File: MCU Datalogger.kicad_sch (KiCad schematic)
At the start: 25 parts, among them U1 24LC1025, U2 24LC1025, U3 DS1337S_, U4 ATMEGA328P-AU, Y1 32.768 KHZ, Y2 16 MHz

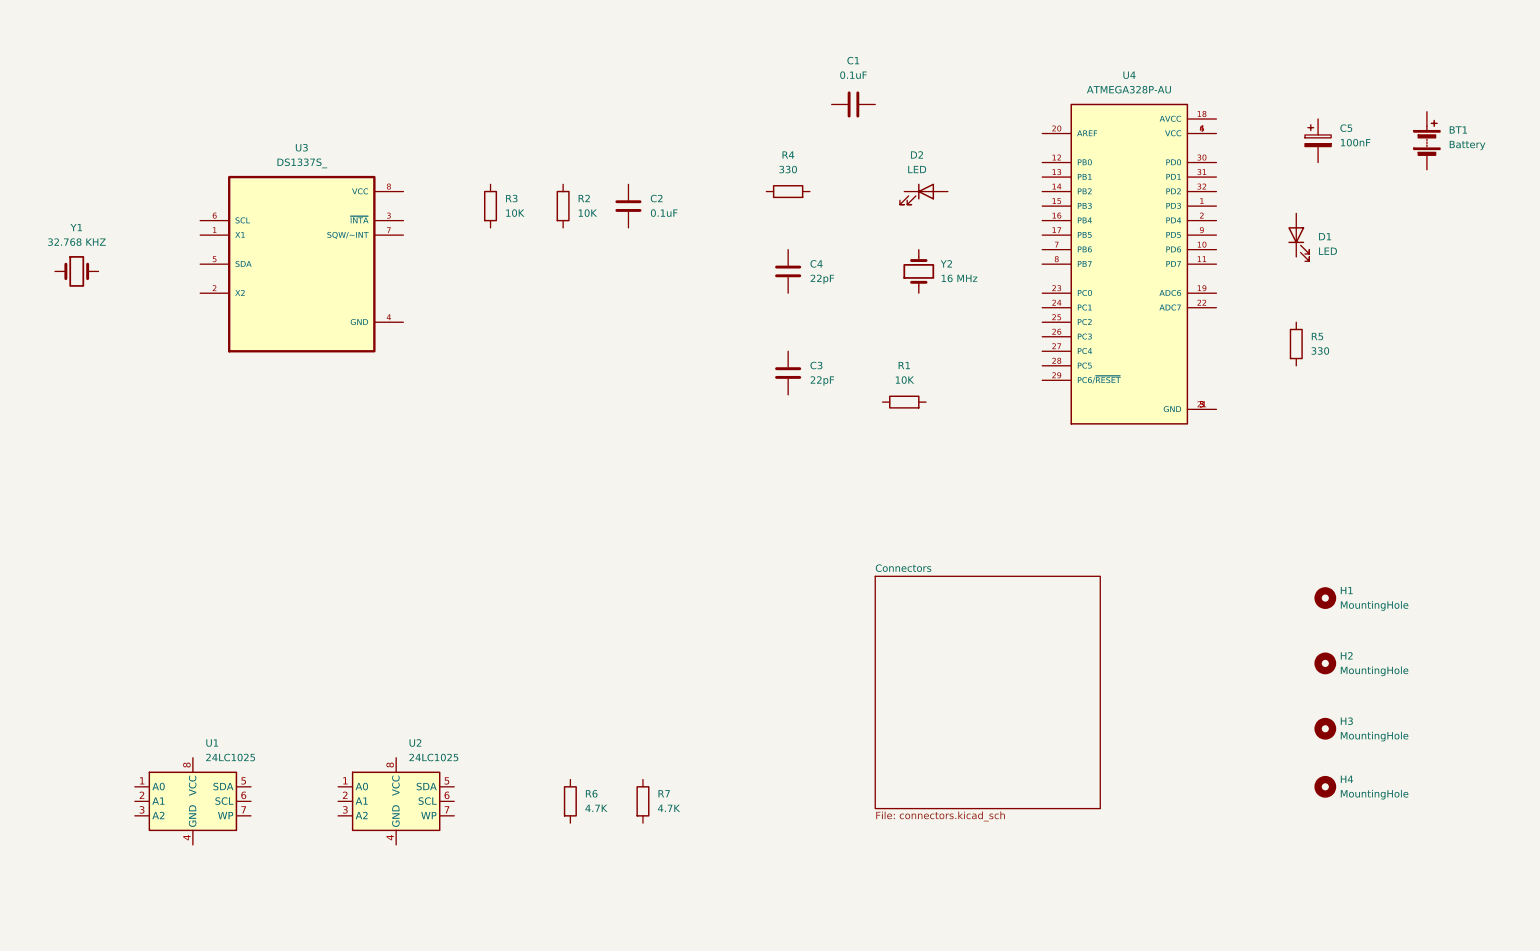
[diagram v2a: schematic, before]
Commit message: Completed wiring of main sheet.
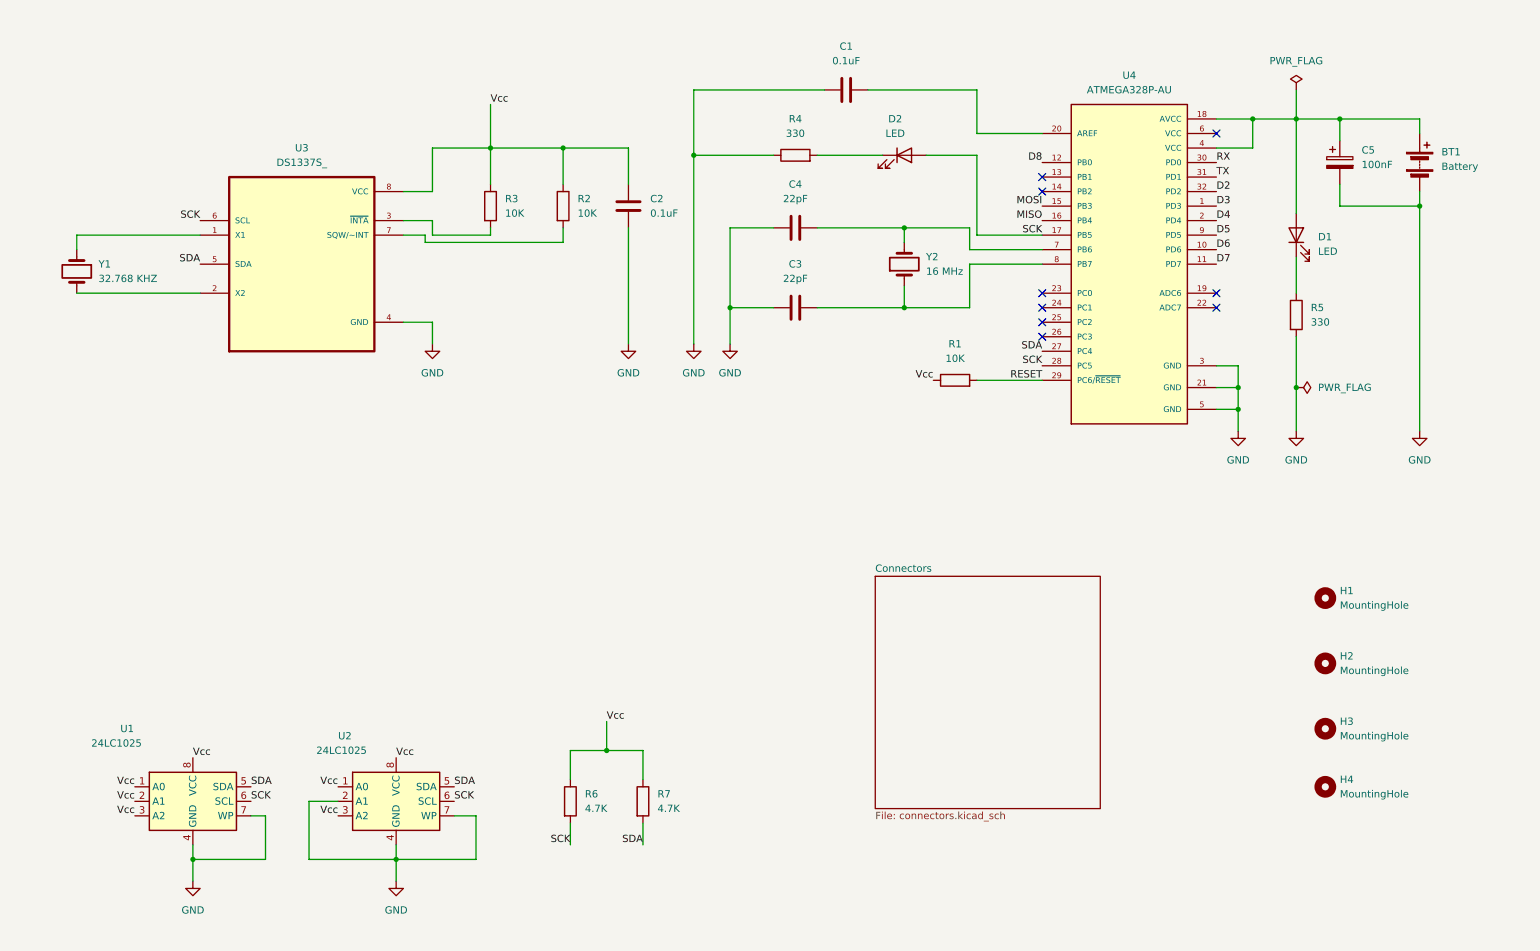
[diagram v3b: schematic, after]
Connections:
- net at R5.1: now also D1.1 (K)
- net GND: now reaches R5.2
- net GND: now also BT1.2 (-), C1.1, C2.2, C3.1, C4.1, C5.2, R4.1, U1.4 (GND), U1.7 (WP), U2.2 (A1), U2.4 (GND), U2.7 (WP), U3.4 (GND), U4.21 (GND), U4.3 (GND), U4.5 (GND)
- net Vcc: now reaches U2.1 (A0)
- net Vcc: now also C2.1, R1.1, R2.1, R3.1, R6.1, R7.1, U1.1 (A0), U1.2 (A1), U1.3 (A2), U1.8 (VCC), U2.3 (A2), U2.8 (VCC), U3.8 (VCC)
- net SDA: now reaches U2.5 (SDA)
- net SDA: now also R7.2, U1.5 (SDA), U3.5 (SDA), U4.27 (PC4)
- net SCK: now reaches U2.6 (SCL)
- net SCK: now also D2.2 (A), R6.2, U1.6 (SCL), U3.6 (SCL), U4.17 (PB5), U4.28 (PC5)
- net at R2.2: now also U3.7 (SQW/~INT)
- net at Y1.1: now also U3.1 (X1)
- net at Y1.2: now also U3.2 (X2)
- net at BT1.1 (+): now also C5.1, D1.2 (A), U4.18 (AVCC), U4.4 (VCC)
- net RESET: now reaches R1.2
- net RESET: now also U4.29 (PC6/~{RESET})
- net at D2.1 (K): now also R4.2
- net at C1.2: now also U4.20 (AREF)
- net at R3.2: now also U3.3 (~{INTA})
- net D3: now reaches U4.1 (PD3)
- net D6: now reaches U4.10 (PD6)
- net D7: now reaches U4.11 (PD7)
- net D8: now reaches U4.12 (PB0)
- net MOSI: now reaches U4.15 (PB3)
- net MISO: now reaches U4.16 (PB4)
- net D4: now reaches U4.2 (PD4)
- net RX: now reaches U4.30 (PD0)
- net TX: now reaches U4.31 (PD1)
- net D2: now reaches U4.32 (PD2)
- net at U4.6 (VCC): no longer U4.4 (VCC)
- net at U4.7 (PB6): now also C4.2, Y2.2
- net at U4.8 (PB7): now also C3.2, Y2.1
- net D5: now reaches U4.9 (PD5)
- no-connect marks 0 -> 9
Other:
- moved on the sheet: BT1, C1, C3, C4, C5, D2, R1, R4, R5, Y1, Y2

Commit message: Completed wiring in second sheet.
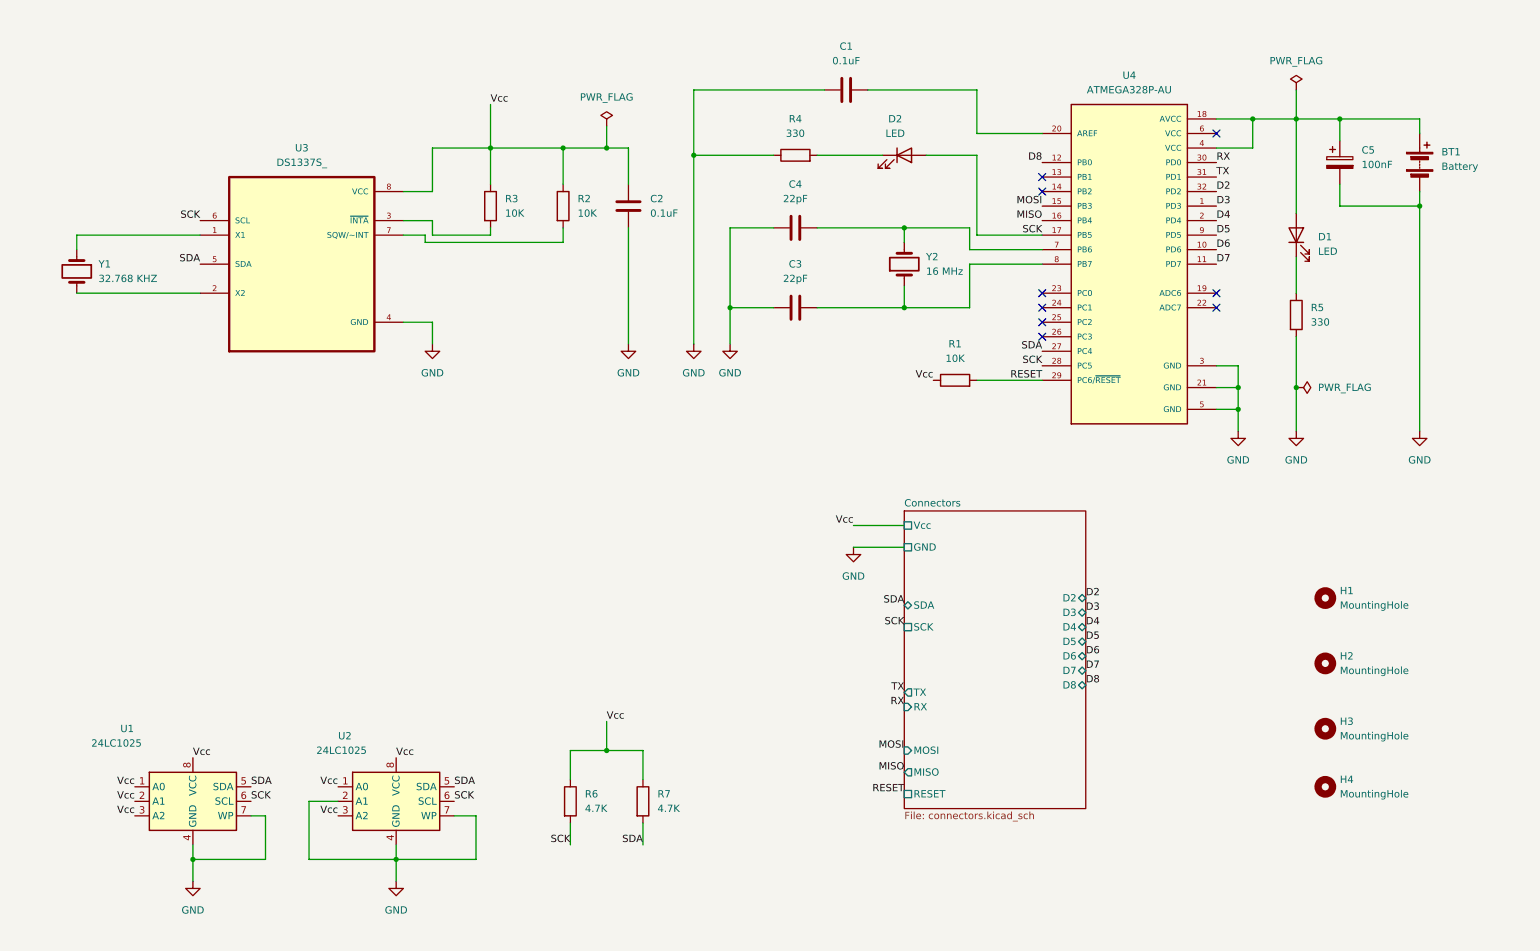
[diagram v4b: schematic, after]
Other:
- sheet Connectors ports: added D2, D3, D4, D5, D6, D7, D8, GND, MISO, MOSI, RESET, RX, SCK, SDA, TX, Vcc; removed none
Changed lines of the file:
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@@
   (junction (at 231.14 80.01) (diameter 0) (color 0 0 0 0)
+  )
+  (junction (at 120.65 38.1) (diameter 0) (color 0 0 0 0)
   )
   (junction (at 248.92 33.02) (diameter 0) (color 0 0 0 0)
@@
     (stroke (width 0) (type default))
   )
-  (wire (pts (xy 124.46 38.1) (xy 113.03 38.1))
+  (wire (pts (xy 124.46 38.1) (xy 120.65 38.1))
     (stroke (width 0) (type default))
   )
@@
     (stroke (width 0) (type default))
   )
+  (wire (pts (xy 163.83 104.14) (xy 172.72 104.14))
+    (stroke (width 0) (type default))
+  )
   (wire (pts (xy 262.89 35.56) (xy 262.89 33.02))
     (stroke (width 0) (type default))
@@
     (stroke (width 0) (type default))
   )
+  (wire (pts (xy 120.65 38.1) (xy 113.03 38.1))
+    (stroke (width 0) (type default))
+  )
   (wire (pts (xy 262.89 48.26) (xy 262.89 87.63))
     (stroke (width 0) (type default))
@@
     (stroke (width 0) (type default))
   )
+  (wire (pts (xy 163.83 107.95) (xy 172.72 107.95))
+    (stroke (width 0) (type default))
+  )
   (wire (pts (xy 114.3 143.51) (xy 120.65 143.51))
     (stroke (width 0) (type default))
@@
     (stroke (width 0) (type default))
   )
+  (wire (pts (xy 120.65 34.29) (xy 120.65 38.1))
+    (stroke (width 0) (type default))
+  )
   (wire (pts (xy 68.58 152.4) (xy 68.58 162.56))
     (stroke (width 0) (type default))
@@
     (effects (font (size 1.27 1.27)) (justify left bottom))
   )
+  (label "RX" (at 172.72 135.89 180) (fields_autoplaced)
+    (effects (font (size 1.27 1.27)) (justify right bottom))
+  )
+  (label "RESET" (at 172.72 151.13 180) (fields_autoplaced)
+    (effects (font (size 1.27 1.27)) (justify right bottom))
+  )
+  (label "D8" (at 204.47 132.08 0) (fields_autoplaced)
+    (effects (font (size 1.27 1.27)) (justify left bottom))
+  )
   (label "SDA" (at 93.98 149.86 0) (fields_autoplaced)
     (effects (font (size 1.27 1.27)) (justify left bottom))
@@
     (effects (font (size 1.27 1.27)) (justify left bottom))
   )
+  (label "SCK" (at 172.72 121.92 180) (fields_autoplaced)
+    (effects (font (size 1.27 1.27)) (justify right bottom))
+  )
   (label "TX" (at 227.33 43.18 0) (fields_autoplaced)
     (effects (font (size 1.27 1.27)) (justify left bottom))
   )
+  (label "D4" (at 204.47 121.92 0) (fields_autoplaced)
+    (effects (font (size 1.27 1.27)) (justify left bottom))
+  )
   (label "Vcc" (at 120.65 138.43 0) (fields_autoplaced)
     (effects (font (size 1.27 1.27)) (justify left bottom))
@@
     (effects (font (size 1.27 1.27)) (justify right bottom))
   )
+  (label "MOSI" (at 172.72 143.51 180) (fields_autoplaced)
+    (effects (font (size 1.27 1.27)) (justify right bottom))
+  )
   (label "Vcc" (at 100.33 30.48 0) (fields_autoplaced)
     (effects (font (size 1.27 1.27)) (justify left bottom))
   )
+  (label "D2" (at 204.47 116.84 0) (fields_autoplaced)
+    (effects (font (size 1.27 1.27)) (justify left bottom))
+  )
   (label "RESET" (at 196.85 78.74 180) (fields_autoplaced)
     (effects (font (size 1.27 1.27)) (justify right bottom))
@@
     (effects (font (size 1.27 1.27)) (justify right bottom))
   )
+  (label "D6" (at 204.47 127 0) (fields_autoplaced)
+    (effects (font (size 1.27 1.27)) (justify left bottom))
+  )
+  (label "D5" (at 204.47 124.46 0) (fields_autoplaced)
+    (effects (font (size 1.27 1.27)) (justify left bottom))
+  )
   (label "Vcc" (at 38.1 149.86 180) (fields_autoplaced)
     (effects (font (size 1.27 1.27)) (justify right bottom))
@@
     (effects (font (size 1.27 1.27)) (justify left bottom))
   )
+  (label "TX" (at 172.72 133.35 180) (fields_autoplaced)
+    (effects (font (size 1.27 1.27)) (justify right bottom))
+  )
+  (label "D3" (at 204.47 119.38 0) (fields_autoplaced)
+    (effects (font (size 1.27 1.27)) (justify left bottom))
+  )
   (label "D8" (at 196.85 40.64 180) (fields_autoplaced)
     (effects (font (size 1.27 1.27)) (justify right bottom))
   )
+  (label "SDA" (at 172.72 118.11 180) (fields_autoplaced)
+    (effects (font (size 1.27 1.27)) (justify right bottom))
+  )
   (label "SCK" (at 93.98 152.4 0) (fields_autoplaced)
     (effects (font (size 1.27 1.27)) (justify left bottom))
   )
+  (label "Vcc" (at 163.83 104.14 180) (fields_autoplaced)
+    (effects (font (size 1.27 1.27)) (justify right bottom))
+  )
   (label "Vcc" (at 38.1 154.94 180) (fields_autoplaced)
     (effects (font (size 1.27 1.27)) (justify right bottom))
@@
     (effects (font (size 1.27 1.27)) (justify right bottom))
   )
+  (label "MISO" (at 172.72 147.32 180) (fields_autoplaced)
+    (effects (font (size 1.27 1.27)) (justify right bottom))
+  )
   (label "Vcc" (at 73.66 154.94 180) (fields_autoplaced)
     (effects (font (size 1.27 1.27)) (justify right bottom))
@@
   (label "SDA" (at 196.85 73.66 180) (fields_autoplaced)
     (effects (font (size 1.27 1.27)) (justify right bottom))
+  )
+  (label "D7" (at 204.47 129.54 0) (fields_autoplaced)
+    (effects (font (size 1.27 1.27)) (justify left bottom))
   )
   (label "MOSI" (at 196.85 48.26 180) (fields_autoplaced)
@@
     )
   )
+  (symbol (lib_id "power:PWR_FLAG") (at 120.65 34.29 0) (unit 1)
+    (in_bom yes) (on_board yes) (dnp no) (fields_autoplaced)
+    (property "Reference" "#FLG03" (at 120.65 32.385 0)
+      (effects (font (size 1.27 1.27)) hide)
+    )
+    (property "Value" "PWR_FLAG" (at 120.65 29.21 0)
+      (effects (font (size 1.27 1.27)))
+    )
+    (property "Footprint" "" (at 120.65 34.29 0)
+      (effects (font (size 1.27 1.27)) hide)
+    )
+    (property "Datasheet" "~" (at 120.65 34.29 0)
+      (effects (font (size 1.27 1.27)) hide)
+    )
+    (pin "1")
+    (instances
+      (project "MCU Datalogger"
+        (path "/a66bfded-f757-4203-836f-6885857c7cf0"
+          (reference "#FLG03") (unit 1)
+        )
+      )
+    )
+  )
   (symbol (lib_id "Device:C") (at 162.56 27.94 90) (unit 1)
     (in_bom yes) (on_board yes) (dnp no) (fields_autoplaced)
@@
         (path "/a66bfded-f757-4203-836f-6885857c7cf0"
           (reference "C1") (unit 1)
+        )
+      )
+    )
+  )
+  (symbol (lib_id "power:GND") (at 163.83 107.95 0) (unit 1)
+    (in_bom yes) (on_board yes) (dnp no) (fields_autoplaced)
+    (property "Reference" "#PWR010" (at 163.83 114.3 0)
+      (effects (font (size 1.27 1.27)) hide)
+    )
+    (property "Value" "GND" (at 163.83 113.03 0)
+      (effects (font (size 1.27 1.27)))
+    )
+    (property "Footprint" "" (at 163.83 107.95 0)
+      (effects (font (size 1.27 1.27)) hide)
+    )
+    (property "Datasheet" "" (at 163.83 107.95 0)
+      (effects (font (size 1.27 1.27)) hide)
+    )
+    (pin "1")
+    (instances
+      (project "MCU Datalogger"
+        (path "/a66bfded-f757-4203-836f-6885857c7cf0"
+          (reference "#PWR010") (unit 1)
         )
       )
@@
     )
   )
-  (sheet (at 167.64 113.03) (size 39.37 40.64) (fields_autoplaced)
+  (sheet (at 172.72 101.6) (size 31.75 52.07) (fields_autoplaced)
     (stroke (width 0.0005) (type solid))
     (fill (color 0 0 0 0.0000))
-    (property "Sheetname" "Connectors" (at 167.64 112.3943 0)
+    (property "Sheetname" "Connectors" (at 172.72 100.9643 0)
       (effects (font (size 1.27 1.27)) (justify left bottom))
     )
-    (property "Sheetfile" "connectors.kicad_sch" (at 167.64 154.1787 0)
+    (property "Sheetfile" "connectors.kicad_sch" (at 172.72 154.1787 0)
       (effects (font (size 1.27 1.27)) (justify left top))
     )
-    (instances
+    (pin "GND" passive (at 172.72 107.95 180)
+      (effects (font (size 1.27 1.27)) (justify left))
+    )
+    (pin "SCK" passive (at 172.72 121.92 180)
+      (effects (font (size 1.27 1.27)) (justify left))
+    )
+    (pin "SDA" bidirectional (at 172.72 118.11 180)
+      (effects (font (size 1.27 1.27)) (justify left))
+    )
+    (pin "Vcc" passive (at 172.72 104.14 180)
+      (effects (font (size 1.27 1.27)) (justify left))
+    )
+    (pin "RX" input (at 172.72 135.89 180)
+      (effects (font (size 1.27 1.27)) (justify left))
+    )
+    (pin "TX" output (at 172.72 133.35 180)
+      (effects (font (size 1.27 1.27)) (justify left))
+    )
+    (pin "D4" bidirectional (at 204.47 121.92 0)
+      (effects (font (size 1.27 1.27)) (justify right))
+    )
+    (pin "D3" bidirectional (at 204.47 119.38 0)
+      (effects (font (size 1.27 1.27)) (justify right))
+    )
+    (pin "D5" bidirectional (at 204.47 124.46 0)
+      (effects (font (size 1.27 1.27)) (justify right))
+    )
+    (pin "D2" bidirectional (at 204.47 116.84 0)
+      (effects (font (size 1.27 1.27)) (justify right))
+    )
+    (pin "D7" bidirectional (at 204.47 129.54 0)
+      (effects (font (size 1.27 1.27)) (justify right))
+    )
+    (pin "D6" bidirectional (at 204.47 127 0)
+      (effects (font (size 1.27 1.27)) (justify right))
+    )
+    (pin "D8" bidirectional (at 204.47 132.08 0)
+      (effects (font (size 1.27 1.27)) (justify right))
+    )
+    (pin "MOSI" input (at 172.72 143.51 180)
+      (effects (font (size 1.27 1.27)) (justify left))
+    )
+    (pin "MISO" output (at 172.72 147.32 180)
+      (effects (font (size 1.27 1.27)) (justify left))
+    )
+    (pin "RESET" passive (at 172.72 151.13 180)
+      (effects (font (size 1.27 1.27)) (justify left))
+    )
+    (instances

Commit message: Completed comments.
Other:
- note added: "EEPROM"
- note added: "MCU"
- note added: "Mounting"
- note added: "Real time clock"
- moved on the sheet: BT1, C1, C2, C3, C4, C5, D1, D2, R1, R2, R3, R4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

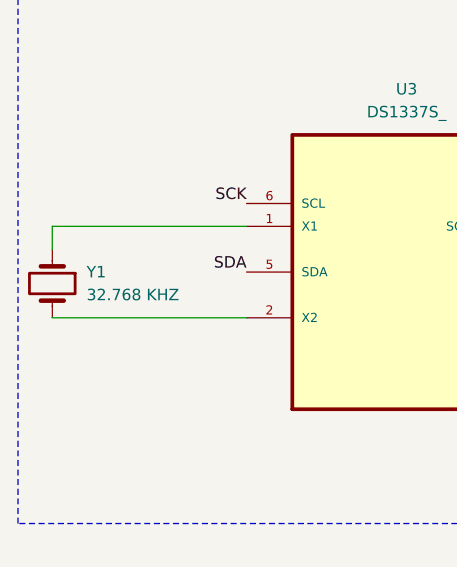
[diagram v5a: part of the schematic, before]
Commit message: Completed placement of footprints.
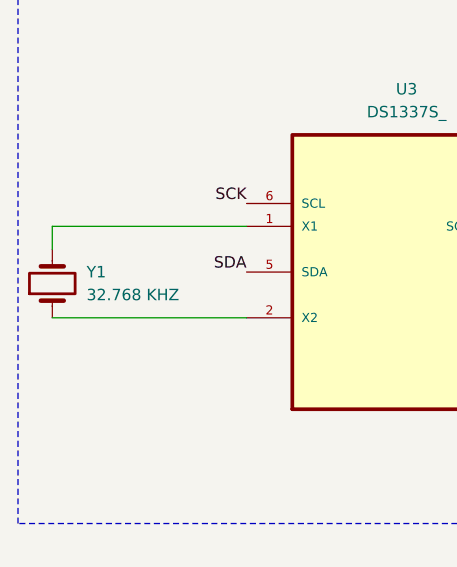
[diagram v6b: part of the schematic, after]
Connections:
- net at Y1.1: now also U3.2 (X2); no longer U3.1 (X1)
- net at Y1.2: now also U3.1 (X1); no longer U3.2 (X2)
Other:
- moved on the sheet: Y1
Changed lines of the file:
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@@
     )
   )
-  (symbol (lib_id "Device:Crystal") (at 20.32 59.69 270) (unit 1)
+  (symbol (lib_id "Device:Crystal") (at 20.32 59.69 90) (unit 1)
     (in_bom yes) (on_board yes) (dnp no) (fields_autoplaced)
     (property "Reference" "Y1" (at 24.13 58.42 90)
-      (effects (font (size 1.27 1.27)) (justify left))
+      (effects (font (size 1.27 1.27)) (justify right))
     )
     (property "Value" "32.768 KHZ" (at 24.13 60.96 90)
-      (effects (font (size 1.27 1.27)) (justify left))
+      (effects (font (size 1.27 1.27)) (justify right))
     )
     (property "Footprint" "Crystal:Crystal_SMD_5032-2Pin_5.0x3.2mm_HandSoldering" (at 20.32 59.69 0)

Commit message: Fixed outstanding issues.
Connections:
- net Vcc: now also BT1.1 (+), C5.1, D1.2 (A), U4.18 (AVCC), U4.4 (VCC)
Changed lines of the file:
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@@
+    (effects (font (size 1.27 1.27)) (justify left bottom))
+  )
+  (label "Vcc" (at 261.62 33.02 0) (fields_autoplaced)
     (effects (font (size 1.27 1.27)) (justify left bottom))
   )
